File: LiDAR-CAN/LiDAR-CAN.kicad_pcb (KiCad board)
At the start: 4 copper layers, 0 parts

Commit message: Start placement of components
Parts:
- added C1: 4.7nF, Capacitor_SMD:C_0603_1608Metric, F.Cu at (101.9, 86.3)
- added C10: 100nF, Capacitor_SMD:C_0603_1608Metric, F.Cu at (90.8, 37.2)
- added C11: 2.2uF, Capacitor_SMD:C_0805_2012Metric, F.Cu at (95.0, 44.0)
- added C12: 22uF, Capacitor_SMD:C_0805_2012Metric, F.Cu at (95.0, 47.0)
- added C13: 22uF, Capacitor_SMD:C_0805_2012Metric, F.Cu at (95.0, 50.0)
- added C14: 10uF, Capacitor_SMD:C_0603_1608Metric, F.Cu at (85.3, 73.5)
- added C15: 100nF, Capacitor_SMD:C_0603_1608Metric, F.Cu at (85.3, 76.0)
- added C16: 100nF, Capacitor_SMD:C_0603_1608Metric, F.Cu at (85.3, 78.5)
- added C17: 10uF, Capacitor_SMD:C_0603_1608Metric, F.Cu at (85.3, 81.1)
- added C18: 100nF, Capacitor_SMD:C_0603_1608Metric, F.Cu at (85.3, 83.6)
- added C19: 100nF, Capacitor_SMD:C_0603_1608Metric, F.Cu at (85.3, 86.1)
- added C2: 1nF, Capacitor_SMD:C_1808_4520Metric, F.Cu at (114.0, 97.0)
- added C20: 10nF, Capacitor_SMD:C_0603_1608Metric, F.Cu at (85.3, 88.6)
- added C21: 10nF, Capacitor_SMD:C_0603_1608Metric, F.Cu at (85.3, 91.1)
- added C22: 8pF, Capacitor_SMD:C_0603_1608Metric, F.Cu at (89.4, 73.5)
- added C23: 8pF, Capacitor_SMD:C_0603_1608Metric, F.Cu at (89.4, 76.0)
- added C24: 10nF, Capacitor_SMD:C_0603_1608Metric, F.Cu at (89.4, 78.5)
- added C25: 4.7uF, Capacitor_SMD:C_0603_1608Metric, F.Cu at (89.4, 81.1)
- added C26: 10uF, Capacitor_SMD:C_0603_1608Metric, F.Cu at (156.7, 109.5)
- added C27: 100nF, Capacitor_SMD:C_0603_1608Metric, F.Cu at (155.2, 109.5)
- added C28: 10uF, Capacitor_SMD:C_0603_1608Metric, F.Cu at (150.7, 109.5)
- added C29: 100nF, Capacitor_SMD:C_0603_1608Metric, F.Cu at (152.2, 109.5)
- added C3: 100pF, Capacitor_SMD:C_0603_1608Metric, F.Cu at (158.9, 112.0)
- added C30: 10uF, Capacitor_SMD:C_0603_1608Metric, F.Cu at (153.7, 109.5)
- added C31: 8pF, Capacitor_SMD:C_0603_1608Metric, F.Cu at (149.3, 115.7)
- added C32: 8pF, Capacitor_SMD:C_0603_1608Metric, F.Cu at (147.3, 113.4)
- added C33: 330nF, Capacitor_SMD:C_0603_1608Metric, F.Cu at (149.2, 109.5)
- added C34: 10uF, Capacitor_SMD:C_0603_1608Metric, F.Cu at (127.8, 38.5)
- added C35: 100nF, Capacitor_SMD:C_0603_1608Metric, F.Cu at (127.8, 41.0)
- added C36: 100nF, Capacitor_SMD:C_0603_1608Metric, F.Cu at (127.8, 43.5)
- added C37: 100nF, Capacitor_SMD:C_0603_1608Metric, F.Cu at (127.8, 46.0)
- added C38: 100nF, Capacitor_SMD:C_0603_1608Metric, F.Cu at (127.8, 48.5)
- added C39: 8pF, Capacitor_SMD:C_0603_1608Metric, F.Cu at (131.8, 38.5)
- added C4: 100pF, Capacitor_SMD:C_0603_1608Metric, F.Cu at (158.9, 115.2)
- added C40: 8pF, Capacitor_SMD:C_0603_1608Metric, F.Cu at (131.8, 41.0)
- added C41: 4.7uF, Capacitor_SMD:C_0603_1608Metric, F.Cu at (131.8, 43.5)
- added C42: 10nF, Capacitor_SMD:C_0603_1608Metric, F.Cu at (131.8, 46.0)
- added C5: 4.7nF, Capacitor_SMD:C_0603_1608Metric, F.Cu at (161.2, 113.7)
- added C6: 100nF, Capacitor_SMD:C_0603_1608Metric, F.Cu at (90.8, 34.7)
- added C7: 2.2uF, Capacitor_SMD:C_0805_2012Metric, F.Cu at (95.0, 35.0)
- added C8: 22uF, Capacitor_SMD:C_0805_2012Metric, F.Cu at (95.0, 38.0)
- added C9: 22uF, Capacitor_SMD:C_0805_2012Metric, F.Cu at (95.0, 41.0)
- added D1: NUP2105L, Package_TO_SOT_SMD:SOT-23, F.Cu at (164.7, 113.7)
- added D2: GREEN, LED_SMD:LED_0603_1608Metric, F.Cu at (107.4, 44.0)
- added D3: 5.1V, Diode_SMD:D_SMA, F.Cu at (101.3, 45.0)
- added D4: GREEN, LED_SMD:LED_0603_1608Metric, F.Cu at (107.4, 46.6)
- added D5: GREEN, LED_SMD:LED_0603_1608Metric, F.Cu at (146.1, 32.2)
- added Dw1: 12V, Diode_SMD:D_SMA, F.Cu at (101.3, 49.6)
- added FB1: MH1608-800Y, Inductor_SMD:L_0603_1608Metric, F.Cu at (89.4, 83.6)
- added FID1: Fiducial, Fiducial:Fiducial_1.5mm_Mask3mm, F.Cu at (66.2, 73.4)
- added FID2: Fiducial, Fiducial:Fiducial_1.5mm_Mask3mm, F.Cu at (66.2, 77.9)
- added H1: MountingHole, MountingHole:MountingHole_2.2mm_M2, F.Cu at (60.9, 74.1)
- added H2: MountingHole, MountingHole:MountingHole_2.2mm_M2, F.Cu at (60.9, 80.0)
- added J1: XT30(2+2), Local_Library:XT30PW(2+2)-M.G.B, F.Cu at (179.8, 76.0)
- added J2: XT30(2+2), Local_Library:XT30PW(2+2)-M.G.B, F.Cu at (120.2, 60.6)
- added J3: G7LX-A88S7-BP-G/Y, Connector_RJ:RJ45_Kycon_G7LX-A88S7-BP-xx_Horizontal, F.Cu at (159.7, 81.8)
- added J4: XT30(2+2), Local_Library:XT30PW(2+2)-M.G.B, F.Cu at (179.9, 119.7)
- added J5: 61300511121, Connector_PinHeader_2.54mm:PinHeader_1x05_P2.54mm_Vertical, F.Cu at (140.1, 39.5)
- added L1: 12uH, Inductor_SMD:L_APV_ANR6020, F.Cu at (106.3, 37.3)
- added L2: 5.6uH, Inductor_SMD:L_APV_ANR3015, F.Cu at (107.7, 50.2)
- added R1: 0R, Resistor_SMD:R_0805_2012Metric, F.Cu at (103.0, 28.1)
- added R10: 59R, Resistor_SMD:R_0603_1608Metric, F.Cu at (161.2, 116.0)
- added R11: 100k, Resistor_SMD:R_0603_1608Metric, F.Cu at (90.8, 39.8)
- added R12: 300R, Resistor_SMD:R_0603_1608Metric, F.Cu at (90.8, 42.3)
- added R13: 5.23k, Resistor_SMD:R_0603_1608Metric, F.Cu at (90.8, 44.8)
- added R14: 100k, Resistor_SMD:R_0603_1608Metric, F.Cu at (90.8, 47.3)
- added R15: 300R, Resistor_SMD:R_0603_1608Metric, F.Cu at (90.8, 49.8)
- added R16: 22.1k, Resistor_SMD:R_0603_1608Metric, F.Cu at (90.8, 52.3)
- added R17: 49.9R, Resistor_SMD:R_0603_1608Metric, F.Cu at (89.4, 86.1)
- added R18: 49.9R, Resistor_SMD:R_0603_1608Metric, F.Cu at (89.4, 88.6)
- added R19: 49.9R, Resistor_SMD:R_0603_1608Metric, F.Cu at (89.4, 91.1)
- added R2: 0R, Resistor_SMD:R_0805_2012Metric, F.Cu at (103.0, 31.0)
- added R20: 49.9R, Resistor_SMD:R_0603_1608Metric, F.Cu at (93.4, 73.5)
- added R21: 10R, Resistor_SMD:R_0603_1608Metric, F.Cu at (93.4, 76.0)
- added R22: 10R, Resistor_SMD:R_0603_1608Metric, F.Cu at (93.4, 78.5)
- added R23: 10k, Resistor_SMD:R_0603_1608Metric, F.Cu at (93.4, 81.1)
- added R24: 10k, Resistor_SMD:R_0603_1608Metric, F.Cu at (93.4, 83.6)
- added R25: 10k, Resistor_SMD:R_0603_1608Metric, F.Cu at (93.4, 86.1)
- added R26: 12.4k, Resistor_SMD:R_0603_1608Metric, F.Cu at (93.4, 88.6)
- added R27: 10k, Resistor_SMD:R_0603_1608Metric, F.Cu at (154.1, 117.7)
- added R28: 10k, Resistor_SMD:R_0603_1608Metric, F.Cu at (155.7, 117.7)
- added R29: 0R, Resistor_SMD:R_0603_1608Metric, F.Cu at (131.8, 48.5)
- added R3: 300R, Resistor_SMD:R_0603_1608Metric, F.Cu at (105.9, 86.3)
- added R30: 0R, Resistor_SMD:R_0603_1608Metric, F.Cu at (135.8, 38.5)
- added R31: 10k, Resistor_SMD:R_0603_1608Metric, F.Cu at (135.8, 41.0)
- added R32: 300R, Resistor_SMD:R_0603_1608Metric, F.Cu at (135.8, 43.5)
- added R33: 10k, Resistor_SMD:R_0603_1608Metric, F.Cu at (135.8, 46.0)
- added R34: 22Ω, Resistor_SMD:R_0805_2012Metric, F.Cu at (146.3, 29.4)
- added R4: 300R, Resistor_SMD:R_0603_1608Metric, F.Cu at (105.9, 88.8)
- added R5: 75R, Resistor_SMD:R_0603_1608Metric, F.Cu at (105.9, 91.3)
- added R6: 75R, Resistor_SMD:R_0603_1608Metric, F.Cu at (105.9, 93.8)
- added R7: 75R, Resistor_SMD:R_0603_1608Metric, F.Cu at (109.9, 86.3)
- added R8: 75R, Resistor_SMD:R_0603_1608Metric, F.Cu at (109.9, 88.8)
- added R9: 59R, Resistor_SMD:R_0603_1608Metric, F.Cu at (161.2, 111.4)
- added SW1: RST, Button_Switch_SMD:SW_SPST_CK_RS282G05A3, F.Cu at (145.7, 25.4)
- added TP1: TestPoint_Small, TestPoint:TestPoint_Pad_D1.0mm, F.Cu at (92.2, 110.8)
- added TP10: TestPoint, TestPoint:TestPoint_Pad_D1.0mm, F.Cu at (83.4, 105.5)
- added TP11: TestPoint, TestPoint:TestPoint_Pad_D1.0mm, F.Cu at (87.0, 102.0)
- added TP12: TestPoint, TestPoint:TestPoint_Pad_D1.0mm, F.Cu at (87.0, 105.5)
- added TP13: TestPoint, TestPoint:TestPoint_Pad_D1.0mm, F.Cu at (90.5, 102.0)
- added TP14: TestPoint, TestPoint:TestPoint_Pad_D1.0mm, F.Cu at (90.5, 105.5)
- added TP15: TestPoint, TestPoint:TestPoint_Pad_D1.0mm, F.Cu at (94.0, 102.0)
- added TP16: TestPoint, TestPoint:TestPoint_Pad_D1.0mm, F.Cu at (94.0, 105.5)
- added TP17: TestPoint, TestPoint:TestPoint_Pad_D1.0mm, F.Cu at (92.5, 119.2)
- added TP18: TestPoint, TestPoint:TestPoint_Pad_D1.0mm, F.Cu at (92.5, 122.7)
- added TP19: TestPoint, TestPoint:TestPoint_Pad_D1.0mm, F.Cu at (96.0, 119.2)
- added TP2: TestPoint_Small, TestPoint:TestPoint_Pad_D1.0mm, F.Cu at (92.2, 113.8)
- added TP20: TestPoint, TestPoint:TestPoint_Pad_D1.0mm, F.Cu at (96.0, 122.7)
- added TP21: TestPoint, TestPoint:TestPoint_Pad_D1.0mm, F.Cu at (99.6, 119.2)
- added TP22: TestPoint, TestPoint:TestPoint_Pad_D1.0mm, F.Cu at (99.6, 122.7)
- added TP23: TestPoint, TestPoint:TestPoint_Pad_D1.0mm, F.Cu at (158.8, 108.2)
- added TP24: TestPoint, TestPoint:TestPoint_Pad_D1.0mm, F.Cu at (148.6, 106.6)
- added TP25: TestPoint, TestPoint:TestPoint_Pad_D1.0mm, F.Cu at (154.7, 106.9)
- added TP26: TestPoint, TestPoint:TestPoint_Pad_D1.0mm, F.Cu at (147.3, 108.5)
- added TP27: TestPoint, TestPoint:TestPoint_Pad_D1.0mm, F.Cu at (149.8, 117.7)
- added TP28: TestPoint, TestPoint:TestPoint_Pad_D1.0mm, F.Cu at (151.9, 117.1)
- added TP29: TestPoint, TestPoint:TestPoint_Pad_D1.0mm, F.Cu at (146.9, 110.7)
- added TP3: TestPoint_Small, TestPoint:TestPoint_Pad_D1.0mm, F.Cu at (95.3, 110.8)
- added TP30: TestPoint, TestPoint:TestPoint_Pad_D1.0mm, F.Cu at (77.8, 102.0)
- added TP31: TestPoint, TestPoint:TestPoint_Pad_D1.0mm, F.Cu at (77.8, 105.5)
- added TP32: TestPoint, TestPoint:TestPoint_Pad_D1.0mm, F.Cu at (77.8, 109.0)
- added TP33: TestPoint, TestPoint:TestPoint_Pad_D1.0mm, F.Cu at (77.8, 112.6)
- added TP34: TestPoint, TestPoint:TestPoint_Pad_D1.0mm, F.Cu at (77.8, 116.2)
- added TP4: TestPoint_Small, TestPoint:TestPoint_Pad_D1.0mm, F.Cu at (95.3, 113.8)
- added TP5: TestPoint_Small, TestPoint:TestPoint_Pad_D1.0mm, F.Cu at (98.3, 110.8)
- added TP6: TestPoint_Small, TestPoint:TestPoint_Pad_D1.0mm, F.Cu at (98.3, 113.8)
- added TP7: TestPoint_Small, TestPoint:TestPoint_Pad_D1.0mm, F.Cu at (101.4, 110.8)
- added TP8: TestPoint_Small, TestPoint:TestPoint_Pad_D1.0mm, F.Cu at (101.4, 113.8)
- added TP9: TestPoint, TestPoint:TestPoint_Pad_D1.0mm, F.Cu at (83.4, 102.0)
- added U1: LMR51430, Package_TO_SOT_SMD:SOT-23-6, F.Cu at (99.8, 35.9)
- added U2: LMR51430, Package_TO_SOT_SMD:SOT-23-6, F.Cu at (99.8, 40.5)
- added U3: W5500, Package_QFP:LQFP-48_7x7mm_P0.5mm, F.Cu at (101.0, 78.0)
- added U4: TCAN4550RGY, Package_DFN_QFN:Texas_RGY_R-PVQFN-N20_EP2.05x3.05mm, F.Cu at (153.9, 113.5)
- added U5: STM32F401RBT6, Package_QFP:LQFP-64_10x10mm_P0.5mm, F.Cu at (133.0, 30.0)
- added Y1: 25MHz, Crystal:Crystal_SMD_2016-4Pin_2.0x1.6mm, F.Cu at (97.3, 85.5)
- added Y2: 40MHz, Crystal:Crystal_SMD_2016-4Pin_2.0x1.6mm, F.Cu at (149.5, 113.4)
- added Y3: 25MHz, Crystal:Crystal_SMD_2016-4Pin_2.0x1.6mm, F.Cu at (142.2, 29.8)
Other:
- board outline added: 60 x 60 mm

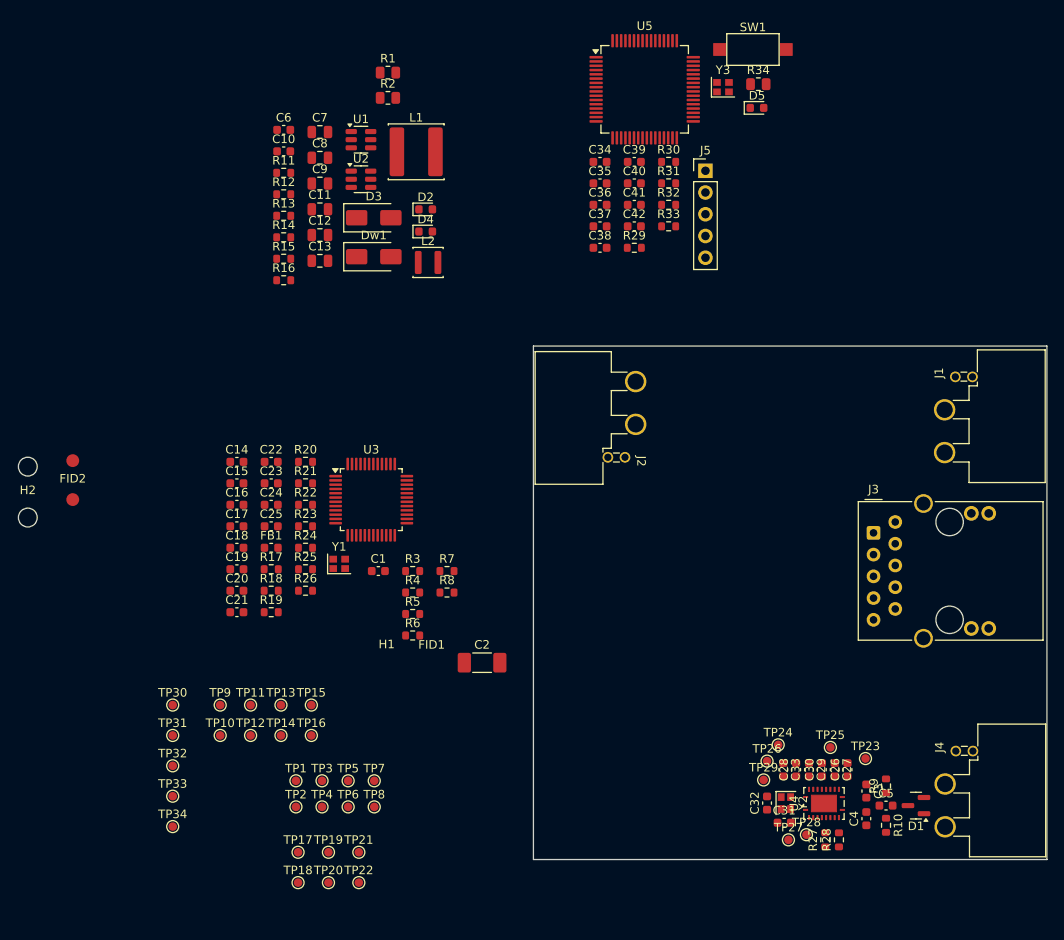
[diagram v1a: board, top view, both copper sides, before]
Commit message: Add CAN and MCU placement
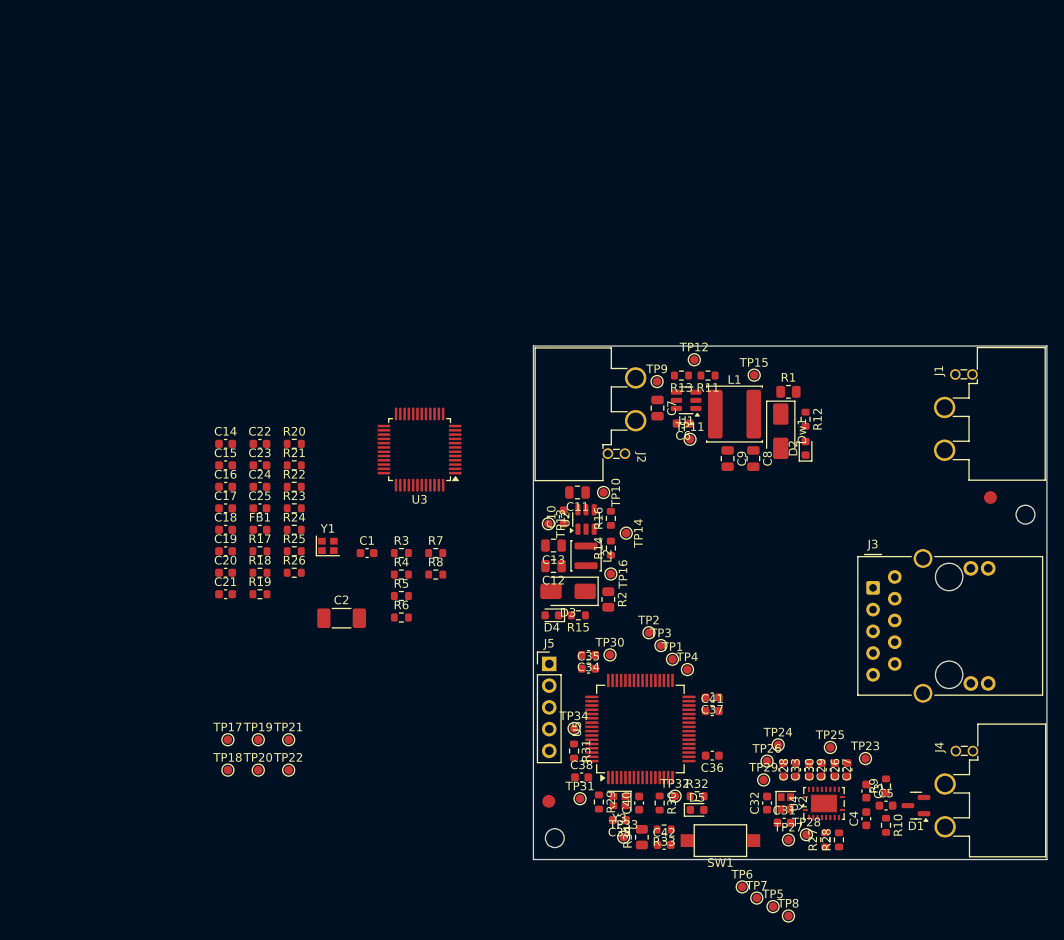
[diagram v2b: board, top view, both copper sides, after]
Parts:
- moved H1 116.7 mm to (177.5, 79.7)
- moved FID1 107.3 mm to (173.4, 77.7)
- moved SW1 92.5 mm to (141.8, 117.8), turned to 180 degrees
- moved R34 89.0 mm to (132.7, 117.4), turned to 90 degrees
- moved Y3 84.3 mm to (130.1, 113.2), turned to 180 degrees
- moved D5 82.3 mm to (139.1, 114.2)
- moved C39 76.9 mm to (130.1, 115.4), turned to 180 degrees
- moved R30 74.9 mm to (134.8, 113.4), turned to -90 degrees
- moved U5 74.8 mm to (132.5, 104.8), turned to 90 degrees
- moved C40 72.4 mm to (132.3, 113.4), turned to 90 degrees
- moved C42 72.4 mm to (135.3, 118.3)
- moved H2 72.1 mm to (122.5, 117.5)
- moved R33 70.5 mm to (135.3, 116.5), turned to 180 degrees
- moved R32 69.2 mm to (139.1, 112.6)
- moved TP12 67.9 mm to (138.8, 61.6)
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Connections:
- U5 pad 14: /Microcontroller/ULED -> unconnected-(U5-PA0-Pad14)
- U5 pad 16: unconnected-(U5-PA2-Pad16) -> /Microcontroller/ULED
- U5 pad 20: /LiDAR Interface/~{SCS} -> /CAN Interface/~{CS}
- U5 pad 21: /LiDAR Interface/SCLK -> /CAN Interface/SCLK
- U5 pad 22: /LiDAR Interface/MISO -> /CAN Interface/SDO
- U5 pad 23: /LiDAR Interface/MOSI -> /CAN Interface/SDI
- U5 pad 25: unconnected-(U5-PC5-Pad25) -> /CAN Interface/~{INT}
- U5 pad 26: unconnected-(U5-PB0-Pad26) -> /CAN Interface/~{WKRQ}
- U5 pad 27: unconnected-(U5-PB1-Pad27) -> /CAN Interface/GPIO2
- U5 pad 28: unconnected-(U5-PB2-Pad28) -> /CAN Interface/GPIO1
- U5 pad 29: unconnected-(U5-PB10-Pad29) -> /CAN Interface/RST
- U5 pad 33: /CAN Interface/~{CS} -> /LiDAR Interface/~{SCS}
- U5 pad 34: /CAN Interface/SCLK -> /LiDAR Interface/SCLK
- U5 pad 35: /CAN Interface/SDI -> /LiDAR Interface/MISO
- U5 pad 36: /CAN Interface/SDO -> /LiDAR Interface/MOSI
- U5 pad 37: /CAN Interface/~{INT} -> unconnected-(U5-PC6-Pad37)
- U5 pad 38: /CAN Interface/RST -> unconnected-(U5-PC7-Pad38)
- U5 pad 51: /CAN Interface/GPIO1 -> unconnected-(U5-PC10-Pad51)
- U5 pad 52: /CAN Interface/GPIO2 -> unconnected-(U5-PC11-Pad52)
- U5 pad 53: /CAN Interface/~{WKRQ} -> unconnected-(U5-PC12-Pad53)

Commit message: Update complete first placement
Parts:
- removed TP20: TestPoint, TestPoint:TestPoint_Pad_D1.0mm
- added H3: MountingHole, MountingHole:MountingHole_2.2mm_M2, F.Cu at (162.3, 105.5)
- moved C21 68.5 mm to (151.9, 98.1), turned to 180 degrees
- moved C20 68.4 mm to (151.9, 94.9), turned to 180 degrees
- moved R4 67.7 mm to (170.3, 103.1)
- moved R3 65.8 mm to (170.3, 82.1)
- moved C2 63.9 mm to (160.7, 81.5)
- moved R18 63.5 mm to (151.4, 90.8), turned to -90 degrees
- moved R19 63.3 mm to (151.4, 87.4), turned to 90 degrees
- moved R22 63.1 mm to (151.9, 96.5)
- moved R21 62.9 mm to (151.9, 93.3)
- moved R17 61.9 mm to (149.5, 91.6), turned to -90 degrees
- moved TP18 59.6 mm to (135.5, 79.1)
- moved R20 59.4 mm to (149.5, 86.6), turned to 90 degrees
- moved C19 57.1 mm to (141.0, 80.3), turned to -90 degrees
- moved C1 57.1 mm to (154.7, 102.3), turned to -90 degrees
- moved TP19 55.5 mm to (138.3, 82.9)
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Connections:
- R19 pad 1: /LiDAR Interface/RXP -> /LiDAR Interface/RXN
- U5 pad 42: unconnected-(U5-PA9-Pad42) -> /LiDAR Interface/~{RST}
- U5 pad 43: unconnected-(U5-PA10-Pad43) -> /LiDAR Interface/~{INT}
- U5 pad 8: /LiDAR Interface/~{INT} -> unconnected-(U5-PC0-Pad8)
- U5 pad 9: /LiDAR Interface/~{RST} -> unconnected-(U5-PC1-Pad9)
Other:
- board size 60 x 60 mm -> 60 x 55 mm

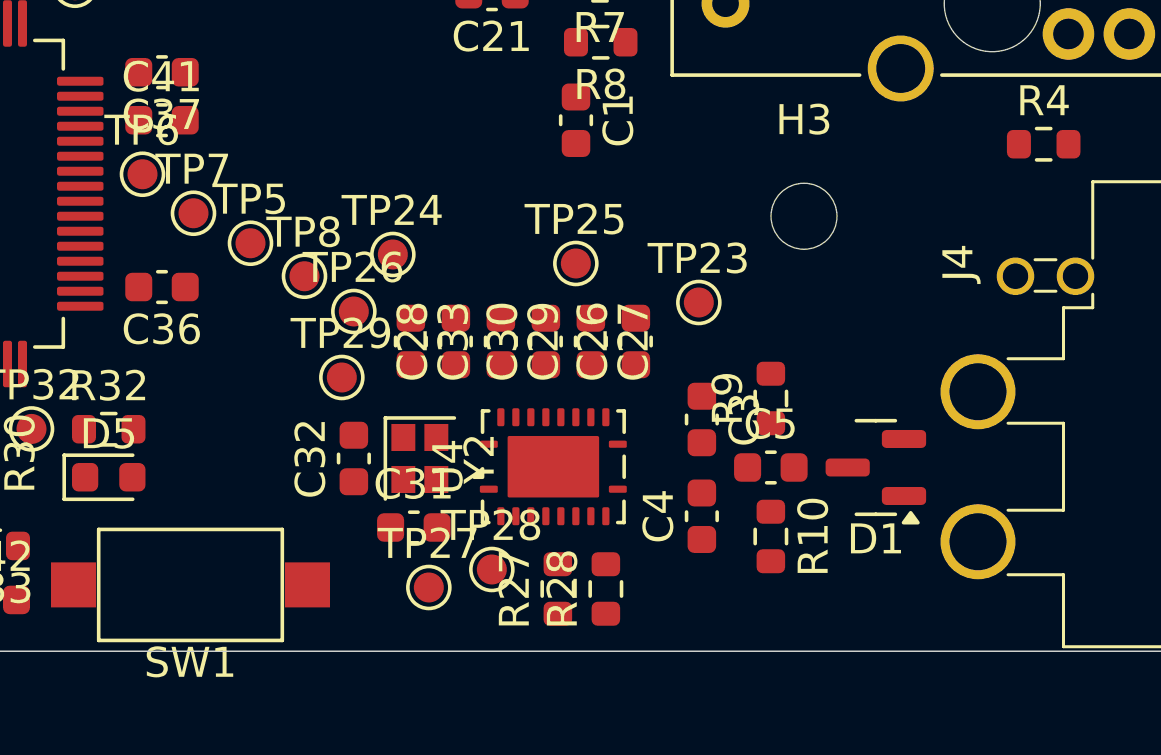
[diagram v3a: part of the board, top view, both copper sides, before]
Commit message: Add CAN interface routing
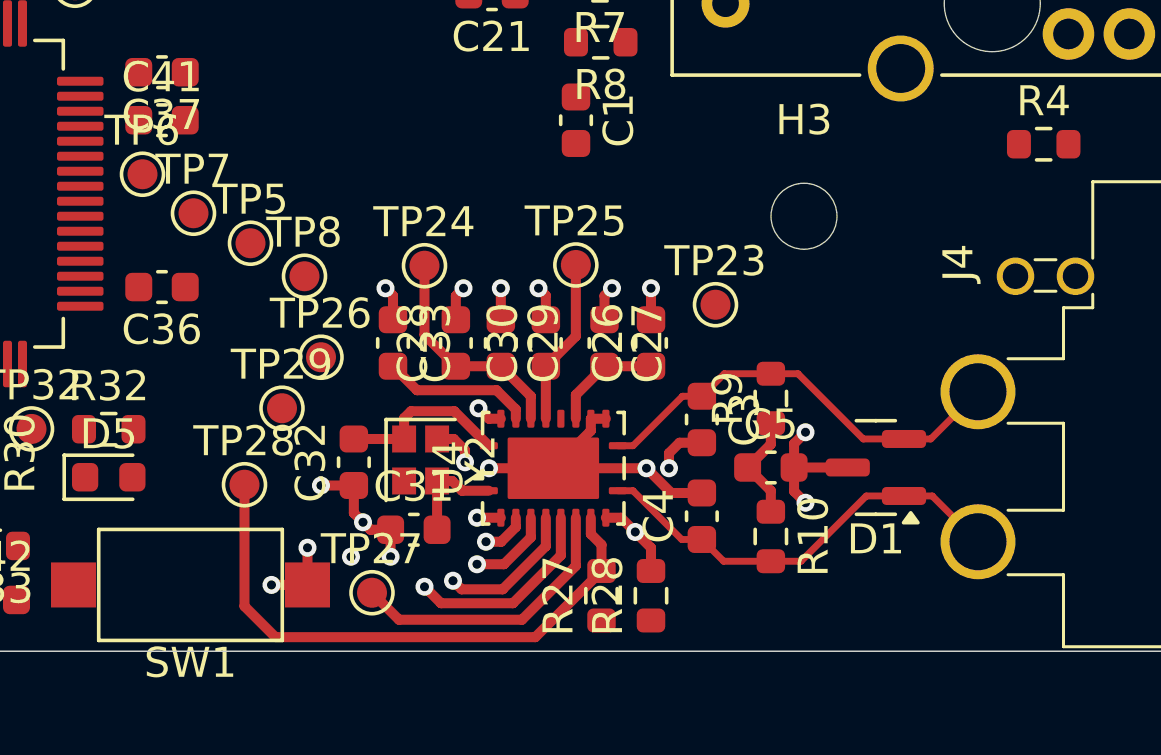
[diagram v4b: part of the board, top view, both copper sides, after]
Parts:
- moved TP28 8.72 mm to (143.7, 114.5)
- moved TP29 2.24 mm to (144.9, 111.9)
- moved TP27 1.90 mm to (147.9, 118.0)
- moved TP26 1.88 mm to (146.2, 110.2)
- moved R28 1.52 mm to (157.2, 118.2)
- moved R27 1.47 mm to (155.6, 118.2)
- moved TP24 1.12 mm to (149.7, 107.2)
- moved C33 0.60 mm to (148.6, 109.7)
- moved TP23 0.56 mm to (159.3, 108.5)
- moved C26 0.51 mm to (157.2, 109.7)
- moved C27 0.46 mm to (155.7, 109.7)
- moved C32 0.12 mm to (147.3, 113.7)
- moved C31 0.08 mm to (149.3, 116.0)
- moved Y2 0.06 mm to (149.5, 113.6)
- moved U4 0.05 mm to (153.9, 113.9)
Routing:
- net GND: track 0.00 -> 31.3 mm, vias 0 -> 17
- net /CAN Interface/~{INT}: track 0.00 -> 19.2 mm
- net /CAN Interface/CAN+: track 0.00 -> 14.6 mm
- net /CAN Interface/CAN-: track 0.00 -> 14.5 mm
- net /CAN Interface/~{CS}: track 0.00 -> 9.52 mm
- net +3.3V: track 0.00 -> 7.45 mm
- net /CAN Interface/SDO: track 0.00 -> 6.69 mm, vias 0 -> 1
- net /CAN Interface/OSC2: track 0.00 -> 5.77 mm
- net /CAN Interface/VCCOUT: track 0.00 -> 5.54 mm
- net /CAN Interface/FLTR: track 0.00 -> 5.00 mm
- net /CAN Interface/SDI: track 0.00 -> 4.76 mm, vias 0 -> 1
- net +12V: track 0.00 -> 3.70 mm
- net Net-(C5-Pad1): track 0.00 -> 3.59 mm
- net /CAN Interface/OSC1: track 0.00 -> 3.46 mm
- net /CAN Interface/SCLK: track 0.00 -> 2.82 mm, vias 0 -> 1
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- added copper zone on In1.Cu, net GND
- added copper zone on In2.Cu, net GND
